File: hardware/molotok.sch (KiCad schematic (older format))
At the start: 16 parts, among them J1 Power, J2 LED, Q1 Q_PMOS_GSD, Q2 DMG9926UDM, SW1 Control, U1 ATtiny85-20SU, U2 AP9101C-SOT-25

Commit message: Reversing mosfet orientation to be correct.
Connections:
- net GND: now also Q2.1 (S); no longer Q2.3 (S)
- net at C1.2, J1.1 (Pin_1), JP1.2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: now also Q2.3 (S); no longer Q2.1 (S)
- net at U2.4 (DO): now also Q2.4 (G); no longer Q2.6 (G)
- net at U2.5 (CO): now also Q2.6 (G); no longer Q2.4 (G)
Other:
- moved on the sheet: Q2A, Q2B
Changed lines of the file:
@@
 	4400 1550 4500 1550
-Wire Wire Line
-	4050 2200 4500 2200
 Wire Wire Line
 	4500 2200 4500 1650
@@
 L coddingtonbear:DMG9926UDM Q2
 U 2 1 5C538EB7
+P 4800 2200
+F 0 "Q2" V 5050 2200 50  0000 C CNN
+F 1 "DMG9926UDM" V 5141 2200 50  0000 C CNN
+F 2 "Package_TO_SOT_SMD:SOT-23-6_Handsoldering" H 5000 2125 50  0001 L CIN
+F 3 "http://www.fairchildsemi.com/ds/FD/FDG1024NZ.pdf" H 4800 2200 50  0001 L CNN
+	2    4800 2200
+	0    1    1    0
+$EndComp
+$Comp
+L coddingtonbear:DMG9926UDM Q2
+U 1 1 5C538F72
 P 5350 2200
 F 0 "Q2" V 5600 2200 50  0000 C CNN
@@
 F 2 "Package_TO_SOT_SMD:SOT-23-6_Handsoldering" H 5550 2125 50  0001 L CIN
 F 3 "http://www.fairchildsemi.com/ds/FD/FDG1024NZ.pdf" H 5350 2200 50  0001 L CNN
-	2    5350 2200
+	1    5350 2200
 	0    -1   1    0
-$EndComp
-$Comp
-L coddingtonbear:DMG9926UDM Q2
-U 1 1 5C538F72
-P 4800 2200
-F 0 "Q2" V 5050 2200 50  0000 C CNN
-F 1 "DMG9926UDM" V 5141 2200 50  0000 C CNN
-F 2 "Package_TO_SOT_SMD:SOT-23-6_Handsoldering" H 5000 2125 50  0001 L CIN
-F 3 "http://www.fairchildsemi.com/ds/FD/FDG1024NZ.pdf" H 4800 2200 50  0001 L CNN
-	1    4800 2200
-	0    1    1    0
 $EndComp
 Wire Wire Line
@@
 Wire Wire Line
 	4050 2650 4050 2200
-Connection ~ 7750 4200
 Wire Wire Line
 	7750 4200 7750 4250
 Wire Wire Line
+	4050 2200 4500 2200
+Wire Wire Line
 	7750 3900 7750 4250

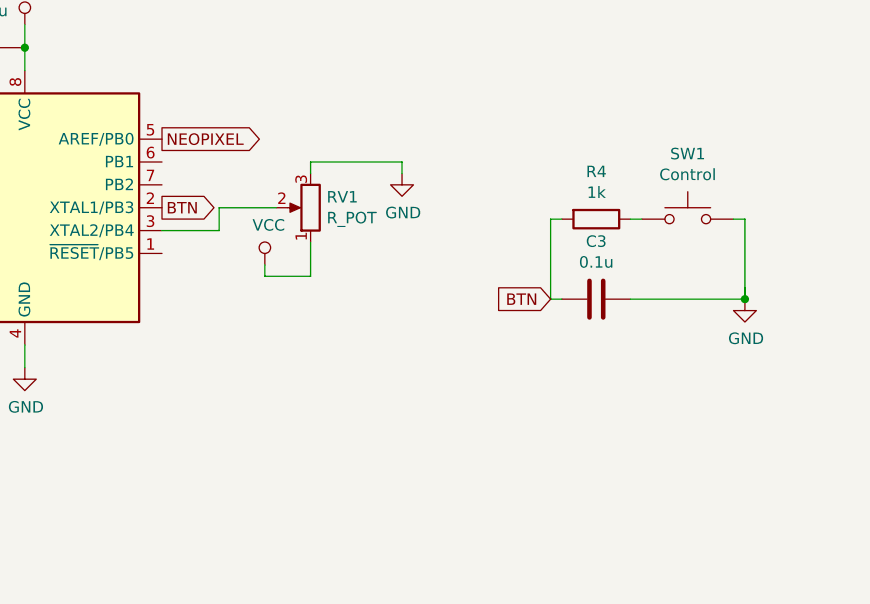
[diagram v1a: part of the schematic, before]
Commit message: Use a rotary encoder instead of a potentiometer for control.
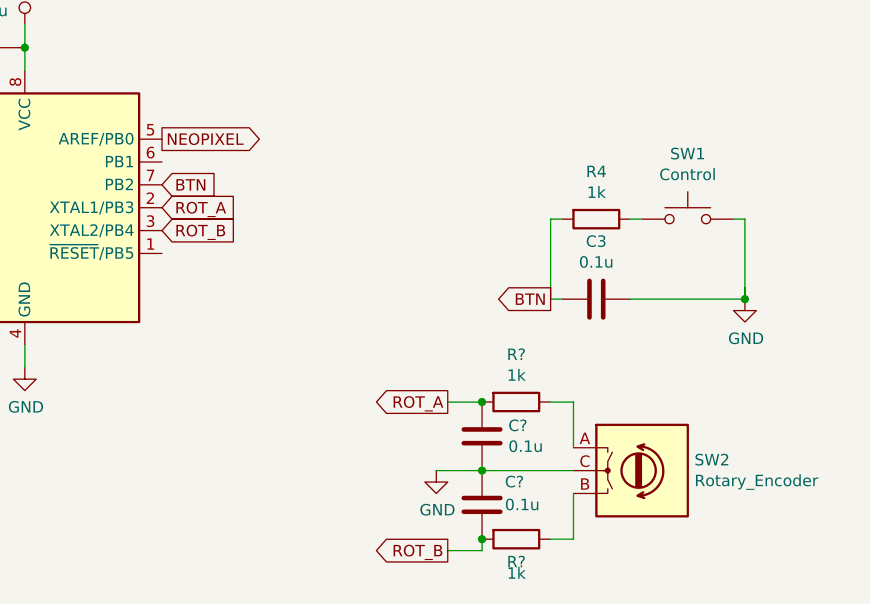
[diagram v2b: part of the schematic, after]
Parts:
- removed RV1: R_POT, coddingtonbear:SV01_Murata_Pot, symbol Device:R_POT
- added C? (x2): 0.1u, coddingtonbear:0805_Milling, symbol Device:C
- added R? (x2): 1k, coddingtonbear:0805_Milling, symbol Device:R
- added SW2: Rotary_Encoder, coddingtonbear:PES12, symbol Device:Rotary_Encoder
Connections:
- net BTN: now also U1.7 (PB2); no longer U1.2 (XTAL1/PB3)
- net GND: now also C?.1, C?.2, SW2.C
- net ROT_B: now reaches U1.3 (XTAL2/PB4)
- net ROT_B: now also C?.2, R?.2
- new net: R?.1, SW2.A
- new net: R?.1, SW2.B
- new net ROT_A: C?.1, R?.2, U1.2 (XTAL1/PB3)
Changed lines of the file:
@@
 NEOPIXEL
-$Comp
-L Device:R_POT RV1
-U 1 1 5C53C20C
-P 5850 3850
-F 0 "RV1" H 5780 3804 50  0000 R CNN
-F 1 "R_POT" H 5780 3895 50  0000 R CNN
-F 2 "coddingtonbear:SV01_Murata_Pot" H 5850 3850 50  0001 C CNN
-F 3 "~" H 5850 3850 50  0001 C CNN
-	1    5850 3850
-	-1   0    0    1
-$EndComp
-$Comp
-L power:VCC #PWR0108
-U 1 1 5C53C2FD
-P 5650 4100
-F 0 "#PWR0108" H 5650 3950 50  0001 C CNN
-F 1 "VCC" H 5667 4273 50  0000 C CNN
-F 2 "" H 5650 4100 50  0001 C CNN
-F 3 "" H 5650 4100 50  0001 C CNN
-	1    5650 4100
-	1    0    0    -1
-$EndComp
-$Comp
-L power:GND #PWR0109
-U 1 1 5C53C322
-P 6250 3700
-F 0 "#PWR0109" H 6250 3450 50  0001 C CNN
-F 1 "GND" H 6255 3527 50  0000 C CNN
-F 2 "" H 6250 3700 50  0001 C CNN
-F 3 "" H 6250 3700 50  0001 C CNN
-	1    6250 3700
-	1    0    0    -1
-$EndComp
 $Comp
 L Switch:SW_Push SW1
@@
 Wire Wire Line
 	6900 4250 6950 4250
-Text GLabel 6900 4250 0    50   Input ~ 0
+Text GLabel 6900 4250 0    50   Output ~ 0
 BTN
-Text GLabel 5200 3850 2    50   Output ~ 0
+Text GLabel 5200 3750 2    50   Input ~ 0
 BTN
-Wire Wire Line
-	5700 3850 5450 3850
-Wire Wire Line
-	5450 3850 5450 3950
-Wire Wire Line
-	5450 3950 5200 3950
-Wire Wire Line
-	5850 3700 5850 3650
-Wire Wire Line
-	5850 3650 6250 3650
-Wire Wire Line
-	6250 3650 6250 3700
-Wire Wire Line
-	5650 4100 5650 4150
-Wire Wire Line
-	5650 4150 5850 4150
-Wire Wire Line
-	5850 4150 5850 4000
 $Comp
 L Device:Jumper_NO_Small JP1
@@
 Wire Wire Line
 	7750 3900 7750 4250
+$Comp
+L Device:Rotary_Encoder SW2
+U 1 1 5C5494FD
+P 7300 5000
+F 0 "SW2" H 7529 5046 50  0000 L CNN
+F 1 "Rotary_Encoder" H 7529 4955 50  0000 L CNN
+F 2 "coddingtonbear:PES12" H 7150 5160 50  0001 C CNN
+F 3 "~" H 7300 5260 50  0001 C CNN
+	1    7300 5000
+	1    0    0    -1
+$EndComp
+$Comp
+L power:GND #PWR0108
+U 1 1 5C549FE7
+P 6400 5000
+F 0 "#PWR0108" H 6400 4750 50  0001 C CNN
+F 1 "GND" H 6405 4827 50  0000 C CNN
+F 2 "" H 6400 5000 50  0001 C CNN
+F 3 "" H 6400 5000 50  0001 C CNN
+	1    6400 5000
+	1    0    0    -1
+$EndComp
+Wire Wire Line
+	7000 5000 6600 5000
+Text GLabel 6450 4700 0    50   Output ~ 0
+ROT_A
+Text GLabel 6450 5350 0    50   Output ~ 0
+ROT_B
+Text GLabel 5200 3950 2    50   Input ~ 0
+ROT_B
+Text GLabel 5200 3850 2    50   Input ~ 0
+ROT_A
+$Comp
+L Device:C C?
+U 1 1 5C54B2D4
+P 6600 4850
+F 0 "C?" H 6715 4896 50  0000 L CNN
+F 1 "0.1u" H 6715 4805 50  0000 L CNN
+F 2 "coddingtonbear:0805_Milling" H 6638 4700 50  0001 C CNN
+F 3 "~" H 6600 4850 50  0001 C CNN
+	1    6600 4850
+	1    0    0    -1
+$EndComp
+$Comp
+L Device:C C?
+U 1 1 5C54B347
+P 6600 5150
+F 0 "C?" H 6700 5250 50  0000 L CNN
+F 1 "0.1u" H 6700 5150 50  0000 L CNN
+F 2 "coddingtonbear:0805_Milling" H 6638 5000 50  0001 C CNN
+F 3 "~" H 6600 5150 50  0001 C CNN
+	1    6600 5150
+	1    0    0    -1
+$EndComp
+Connection ~ 6600 5000
+Wire Wire Line
+	6400 5000 6600 5000
+$Comp
+L Device:R R?
+U 1 1 5C54B480
+P 6750 4700
+F 0 "R?" V 6543 4700 50  0000 C CNN
+F 1 "1k" V 6634 4700 50  0000 C CNN
+F 2 "coddingtonbear:0805_Milling" V 6680 4700 50  0001 C CNN
+F 3 "~" H 6750 4700 50  0001 C CNN
+	1    6750 4700
+	0    1    1    0
+$EndComp
+$Comp
+L Device:R R?
+U 1 1 5C54B4DC
+P 6750 5300
+F 0 "R?" V 6850 5300 50  0000 C CNN
+F 1 "1k" V 6900 5300 50  0000 C CNN
+F 2 "coddingtonbear:0805_Milling" V 6680 5300 50  0001 C CNN
+F 3 "~" H 6750 5300 50  0001 C CNN
+	1    6750 5300
+	0    1    1    0
+$EndComp
+Wire Wire Line
+	6600 4700 6450 4700
+Connection ~ 6600 4700
+Wire Wire Line
+	6450 5350 6600 5350
+Wire Wire Line
+	6600 5350 6600 5300
+Connection ~ 6600 5300
+Wire Wire Line
+	7000 5100 7000 5300
+Wire Wire Line
+	7000 5300 6900 5300
+Wire Wire Line
+	7000 4900 7000 4700
+Wire Wire Line
+	7000 4700 6900 4700
 $EndSCHEMATC

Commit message: Adding firmware.
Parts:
- gave numbers to parts that had none: 4
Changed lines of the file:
@@
 ROT_A
 $Comp
-L Device:C C?
+L Device:C C4
 U 1 1 5C54B2D4
 P 6600 4850
-F 0 "C?" H 6715 4896 50  0000 L CNN
+F 0 "C4" H 6715 4896 50  0000 L CNN
 F 1 "0.1u" H 6715 4805 50  0000 L CNN
 F 2 "coddingtonbear:0805_Milling" H 6638 4700 50  0001 C CNN
@@
 $EndComp
 $Comp
-L Device:C C?
+L Device:C C5
 U 1 1 5C54B347
 P 6600 5150
-F 0 "C?" H 6700 5250 50  0000 L CNN
+F 0 "C5" H 6700 5250 50  0000 L CNN
 F 1 "0.1u" H 6700 5150 50  0000 L CNN
 F 2 "coddingtonbear:0805_Milling" H 6638 5000 50  0001 C CNN
@@
 	6400 5000 6600 5000
 $Comp
-L Device:R R?
+L Device:R R5
 U 1 1 5C54B480
 P 6750 4700
-F 0 "R?" V 6543 4700 50  0000 C CNN
+F 0 "R5" V 6543 4700 50  0000 C CNN
 F 1 "1k" V 6634 4700 50  0000 C CNN
 F 2 "coddingtonbear:0805_Milling" V 6680 4700 50  0001 C CNN
@@
 $EndComp
 $Comp
-L Device:R R?
+L Device:R R6
 U 1 1 5C54B4DC
 P 6750 5300
-F 0 "R?" V 6850 5300 50  0000 C CNN
+F 0 "R6" V 6850 5300 50  0000 C CNN
 F 1 "1k" V 6900 5300 50  0000 C CNN
 F 2 "coddingtonbear:0805_Milling" V 6680 5300 50  0001 C CNN

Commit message: Adding fuse.
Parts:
- added F1: Fuse, Resistor_SMD:R_1206_3216Metric_Pad1.42x1.75mm_HandSolder, symbol Device:Fuse
- added Q3: Q_NMOS_SGD, coddingtonbear:PSMN5R4-25YLD, symbol Device:Q_NMOS_SGD
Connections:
- net GND: now also Q3.1 (S); no longer J2.1 (Pin_1)
- net VCC: now also F1.1; no longer J1.2 (Pin_2)
- net ENABLE_NEOPIXEL: now reaches U1.6 (PB1)
- net ENABLE_NEOPIXEL: now also Q3.2 (G)
- new net: F1.2, J1.2 (Pin_2)
- new net: J2.1 (Pin_1), Q3.3 (D)
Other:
- moved on the sheet: J1
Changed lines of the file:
@@
 EESchema Schematic File Version 4
+LIBS:molotok-cache
 EELAYER 26 0
 EELAYER END
@@
 L Connector_Generic:Conn_01x02 J1
 U 1 1 5C537995
-P 2950 1650
-F 0 "J1" V 2823 1730 50  0000 L CNN
-F 1 "Power" V 2914 1730 50  0000 L CNN
-F 2 "coddingtonbear:JST_XH_B02B-XH-A_02x2.50mm_Straight_LargePads" H 2950 1650 50  0001 C CNN
-F 3 "~" H 2950 1650 50  0001 C CNN
-	1    2950 1650
+P 2350 1650
+F 0 "J1" V 2223 1730 50  0000 L CNN
+F 1 "Power" V 2314 1730 50  0000 L CNN
+F 2 "coddingtonbear:JST_XH_B02B-XH-A_02x2.50mm_Straight_LargePads" H 2350 1650 50  0001 C CNN
+F 3 "~" H 2350 1650 50  0001 C CNN
+	1    2350 1650
 	-1   0    0    1
 $EndComp
@@
 L power:GND #PWR0101
 U 1 1 5C537BC5
-P 8000 2450
-F 0 "#PWR0101" H 8000 2200 50  0001 C CNN
-F 1 "GND" H 8005 2277 50  0000 C CNN
-F 2 "" H 8000 2450 50  0001 C CNN
-F 3 "" H 8000 2450 50  0001 C CNN
-	1    8000 2450
+P 9300 2750
+F 0 "#PWR0101" H 9300 2500 50  0001 C CNN
+F 1 "GND" H 9305 2577 50  0000 C CNN
+F 2 "" H 9300 2750 50  0001 C CNN
+F 3 "" H 9300 2750 50  0001 C CNN
+	1    9300 2750
 	1    0    0    -1
 $EndComp
@@
 Wire Wire Line
 	7700 2450 7700 2300
-Wire Wire Line
-	7700 2300 8000 2300
-Wire Wire Line
-	8000 2300 8000 2450
-Wire Wire Line
-	3150 1650 3200 1650
 Wire Wire Line
 	3200 1650 3200 2200
@@
 $EndComp
 Wire Wire Line
-	3150 1550 3350 1550
-Wire Wire Line
 	3750 1850 3750 2200
 Wire Wire Line
@@
 Wire Wire Line
 	7000 4700 6900 4700
+$Comp
+L Device:Q_NMOS_SGD Q3
+U 1 1 5C55C590
+P 9200 2550
+F 0 "Q3" H 9405 2596 50  0000 L CNN
+F 1 "Q_NMOS_SGD" H 9405 2505 50  0000 L CNN
+F 2 "coddingtonbear:PSMN5R4-25YLD" H 9400 2650 50  0001 C CNN
+F 3 "~" H 9200 2550 50  0001 C CNN
+	1    9200 2550
+	1    0    0    -1
+$EndComp
+Text GLabel 5200 3650 2    50   Output ~ 0
+ENABLE_NEOPIXEL
+Wire Wire Line
+	9300 2300 9300 2350
+Wire Wire Line
+	7700 2300 9300 2300
+Text GLabel 9000 2550 0    50   Input ~ 0
+ENABLE_NEOPIXEL
+$Comp
+L Device:Fuse F1
+U 1 1 5C55F5C3
+P 2850 1550
+F 0 "F1" V 2653 1550 50  0000 C CNN
+F 1 "Fuse" V 2744 1550 50  0000 C CNN
+F 2 "Resistor_SMD:R_1206_3216Metric_Pad1.42x1.75mm_HandSolder" V 2780 1550 50  0001 C CNN
+F 3 "~" H 2850 1550 50  0001 C CNN
+	1    2850 1550
+	0    1    1    0
+$EndComp
+Wire Wire Line
+	2700 1550 2550 1550
+Wire Wire Line
+	3000 1550 3350 1550
+Wire Wire Line
+	2550 1650 3200 1650
 $EndSCHEMATC
